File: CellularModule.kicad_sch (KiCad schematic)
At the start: 1 part, among them U9 BG95-M3

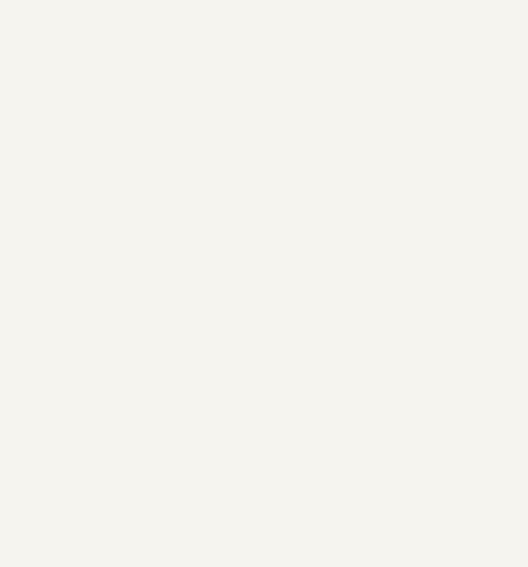
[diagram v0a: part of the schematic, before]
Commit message: full initial power scheme
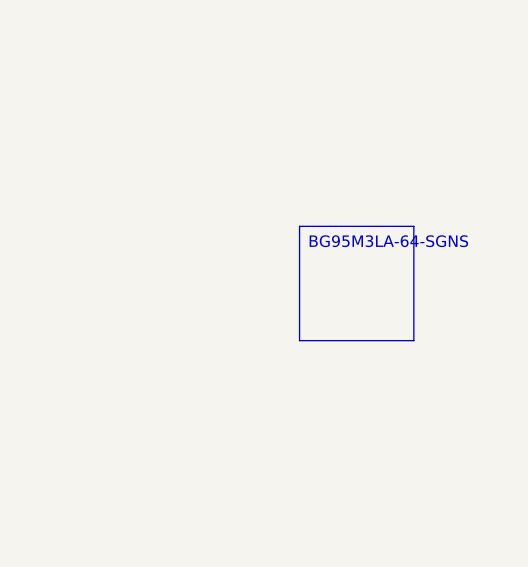
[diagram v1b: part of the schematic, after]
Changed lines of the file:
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@@
 	(generator_version "9.0")
 	(paper "A4")
+	(text_box "BG95M3LA-64-SGNS"
+		(exclude_from_sim no)
+		(at 190.5 76.2 0)
+		(size 12.7 12.7)
+		(margins 0.9525 0.9525 0.9525 0.9525)
+		(stroke
+			(width 0)
+			(type solid)
+		)
+		(fill
+			(type none)
+		)
+		(effects
+			(font
+				(size 1.27 1.27)
+			)
+			(justify left top)
+		)
+	)
 	(symbol
 		(lib_id "RF_GSM:BG95-M3")

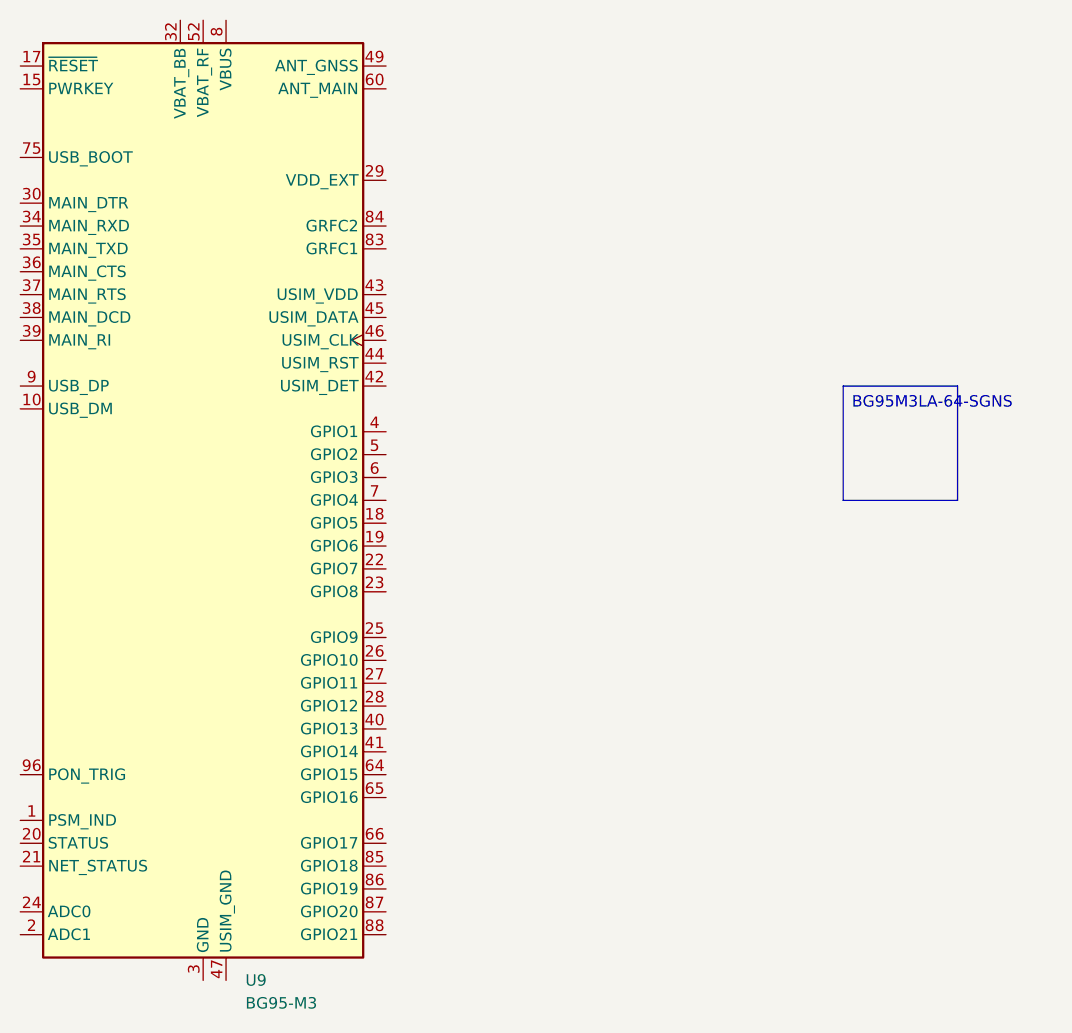
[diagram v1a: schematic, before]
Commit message: added connects schematic, which is looking quite good
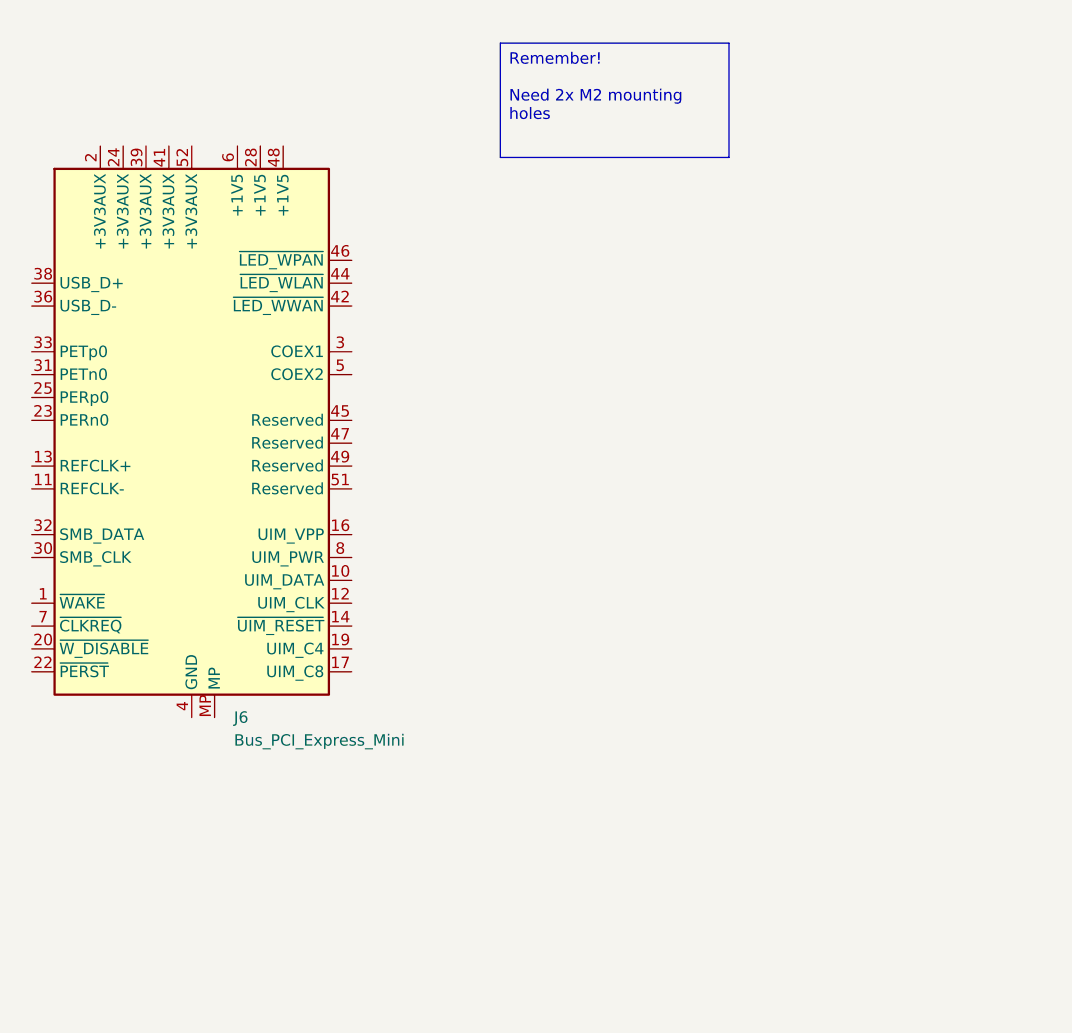
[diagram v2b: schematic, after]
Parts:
- removed U9: BG95-M3, RF_GSM:Quectel_BG95, symbol RF_GSM:BG95-M3
- added J6: Bus_PCI_Express_Mini, Connector_PCBEdge:BUS_PCI_Express_Mini_Full, symbol Connector:Bus_PCI_Express_Mini
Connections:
- new net: J6.15 (GND), J6.18 (GND), J6.21 (GND), J6.26 (GND), J6.27 (GND), J6.29 (GND), J6.34 (GND), J6.35 (GND), J6.37 (GND), J6.4 (GND), J6.40 (GND), J6.43 (GND), J6.50 (GND), J6.9 (GND)
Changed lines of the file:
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@@
 	(generator_version "9.0")
 	(paper "A4")
-	(text_box "BG95M3LA-64-SGNS"
+	(text_box "Remember!\n\nNeed 2x M2 mounting holes"
 		(exclude_from_sim no)
-		(at 190.5 76.2 0)
-		(size 12.7 12.7)
+		(at 152.4 38.1 0)
+		(size 25.4 12.7)
 		(margins 0.9525 0.9525 0.9525 0.9525)
 		(stroke
@@
 		(effects
 			(font
+				(face "KiCad Font")
 				(size 1.27 1.27)
 			)
@@
 	)
 	(symbol
-		(lib_id "RF_GSM:BG95-M3")
-		(at 119.38 88.9 0)
+		(lib_id "Connector:Bus_PCI_Express_Mini")
+		(at 118.11 82.55 0)
 		(unit 1)
 		(exclude_from_sim no)
@@
 		(dnp no)
 		(fields_autoplaced yes)
-		(property "Reference" "U9"
-			(at 124.0633 142.24 0)
+		(property "Reference" "J6"
+			(at 122.7933 113.03 0)
 			(effects
 				(font
@@
 			)
 		)
-		(property "Value" "BG95-M3"
-			(at 124.0633 144.78 0)
+		(property "Value" "Bus_PCI_Express_Mini"
+			(at 122.7933 115.57 0)
 			(effects
 				(font
@@
 			)
 		)
-		(property "Footprint" "RF_GSM:Quectel_BG95"
-			(at 119.38 146.304 0)
+		(property "Footprint" "Connector_PCBEdge:BUS_PCI_Express_Mini_Full"
+			(at 118.11 82.55 0)
 			(effects
 				(font
@@
 			)
 		)
-		(property "Datasheet" "https://images.quectel.com/python/sites/2/2023/05/Quectel_BG95_Series_QuecOpen_Hardware_Design_V1.3.pdf"
-			(at 119.38 60.96 0)
+		(property "Datasheet" "~"
+			(at 114.3 111.76 0)
 			(effects
 				(font
@@
 			)
 		)
-		(property "Description" "NB-IoT, Cat M1 Cat NB2 EGPRS Communication Module, AT Command Set"
-			(at 119.38 60.96 0)
+		(property "Description" "Mini-PCI Express bus connector"
+			(at 118.11 82.55 0)
 			(effects
 				(font
@@
 			)
 		)
-		(pin "30"
+		(pin "38"
+		)
+		(pin "33"
+		)
+		(pin "15"
+		)
+		(pin "26"
+		)
+		(pin "37"
+		)
+		(pin "20"
+		)
+		(pin "11"
+		)
+		(pin "32"
+		)
+		(pin "7"
 		)
 		(pin "36"
 		)
-		(pin "11"
+		(pin "39"
+		)
+		(pin "31"
+		)
+		(pin "35"
+		)
+		(pin "24"
+		)
+		(pin "25"
+		)
+		(pin "27"
+		)
+		(pin "34"
+		)
+		(pin "1"
+		)
+		(pin "23"
+		)
+		(pin "4"
+		)
+		(pin "30"
 		)
 		(pin "13"
 		)
+		(pin "2"
+		)
+		(pin "22"
+		)
+		(pin "18"
+		)
+		(pin "41"
+		)
+		(pin "52"
+		)
+		(pin "21"
+		)
+		(pin "29"
+		)
+		(pin "43"
+		)
+		(pin "50"
+		)
+		(pin "40"
+		)
+		(pin "9"
+		)
+		(pin "3"
+		)
+		(pin "48"
+		)
+		(pin "49"
+		)
+		(pin "16"
+		)
+		(pin "42"
+		)
+		(pin "46"
+		)
+		(pin "6"
+		)
+		(pin "5"
+		)
+		(pin "47"
+		)
 		(pin "51"
 		)
-		(pin "35"
+		(pin "MP"
 		)
-		(pin "15"
+		(pin "12"
 		)
-		(pin "75"
+		(pin "19"
+		)
+		(pin "17"
+		)
+		(pin "44"
+		)
+		(pin "45"
+		)
+		(pin "28"
+		)
+		(pin "14"
+		)
+		(pin "8"
 		)
 		(pin "10"
 		)
-		(pin "39"
-		)
-		(pin "9"
-		)
-		(pin "96"
-		)
-		(pin "20"
-		)
-		(pin "21"
-		)
-		(pin "37"
-		)
-		(pin "38"
-		)
-		(pin "17"
-		)
-		(pin "1"
-		)
-		(pin "24"
-		)
-		(pin "34"
-		)
-		(pin "2"
-		)
-		(pin "12"
-		)
-		(pin "14"
-		)
-		(pin "16"
-		)
-		(pin "100"
-		)
-		(pin "92"
-		)
-		(pin "97"
-		)
-		(pin "52"
-		)
-		(pin "57"
-		)
-		(pin "77"
-		)
-		(pin "94"
-		)
-		(pin "98"
-		)
-		(pin "58"
-		)
-		(pin "76"
-		)
-		(pin "93"
-		)
-		(pin "54"
-		)
-		(pin "102"
-		)
-		(pin "59"
-		)
-		(pin "63"
-		)
-		(pin "69"
-		)
-		(pin "67"
-		)
-		(pin "95"
-		)
-		(pin "32"
-		)
-		(pin "70"
-		)
-		(pin "33"
-		)
-		(pin "50"
-		)
-		(pin "61"
-		)
-		(pin "78"
-		)
-		(pin "53"
-		)
-		(pin "31"
-		)
-		(pin "3"
-		)
-		(pin "101"
-		)
-		(pin "48"
-		)
-		(pin "55"
-		)
-		(pin "62"
-		)
-		(pin "68"
-		)
-		(pin "72"
-		)
-		(pin "47"
-		)
-		(pin "46"
-		)
-		(pin "4"
-		)
-		(pin "60"
-		)
-		(pin "29"
-		)
-		(pin "45"
-		)
-		(pin "22"
-		)
-		(pin "79"
-		)
-		(pin "99"
-		)
-		(pin "56"
-		)
-		(pin "44"
-		)
-		(pin "6"
-		)
-		(pin "80"
-		)
-		(pin "89"
-		)
-		(pin "73"
-		)
-		(pin "81"
-		)
-		(pin "71"
-		)
-		(pin "82"
-		)
-		(pin "8"
-		)
-		(pin "49"
-		)
-		(pin "84"
-		)
-		(pin "90"
-		)
-		(pin "91"
-		)
-		(pin "74"
-		)
-		(pin "83"
-		)
-		(pin "43"
-		)
-		(pin "42"
-		)
-		(pin "5"
-		)
-		(pin "7"
-		)
-		(pin "18"
-		)
-		(pin "19"
-		)
-		(pin "40"
-		)
-		(pin "85"
-		)
-		(pin "25"
-		)
-		(pin "28"
-		)
-		(pin "41"
-		)
-		(pin "64"
-		)
-		(pin "66"
-		)
-		(pin "23"
-		)
-		(pin "27"
-		)
-		(pin "86"
-		)
-		(pin "87"
-		)
-		(pin "65"
-		)
-		(pin "88"
-		)
-		(pin "26"
-		)
 		(instances
-			(project "NCU"
+			(project ""
 				(path "/3aee14c3-5480-4f7c-989e-3fef81779034/77f505d1-5a70-4b67-92f2-4570e0aae5e4"
-					(reference "U9")
+					(reference "J6")
 					(unit 1)
 				)
